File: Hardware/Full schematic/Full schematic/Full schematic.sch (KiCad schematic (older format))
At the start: 145 parts, among them J1 Conn_01x04_Male, J4 Conn_01x02_Male, J6 Conn_01x02_Male, J7 Conn_01x02_Male, J8 Conn_01x07_Male, K1 EDR101A0500, K2 EDR101A0500, K3 EDR101A0500, K4 EDR101A0500, K5 EDR101A0500, K6 EDR101A0500, Q1 BSS138, Q2 IRF610, Q3 IRLML2502, Q4 IRLML2502, Q5 IRLML2502, Q6 IRLML2502, Q7 IRLML2502, Q8 IRLML2502, U1 74LVC2T45DC, U2 74LVC2T45DC, U3 AD9835, X1 50MHz

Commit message: 144MHz preamp is ready
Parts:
- added C?: 1nF, symbol Device:C
- added C?: 75pF, symbol Device:C
- added L?: 200nH, symbol Device:L
- added Q?: BFS17, symbol Device:Q_NPN_BEC
- added R?: 1k, symbol Device:R
- added R?: 6.2k, symbol Device:R
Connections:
- wire segments 369 -> 385
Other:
- note added: "144-146MHz\n1.5V P-P\n8.5mW @ 33 Ohm"
- note added: "200V P-P at antenna equivalent.\nAntenna equivalent is 240 Ohm resistor\nin series with 35pF capacitor."
- note added: "4.32V P-P\n@\n10 Ohm"
- note added: "6T\nD5\nd0.5"
- note added: "M50BH\n20x12x6 ring"
- note removed: "144-146MHz 1.5V P-P"
- note removed: "200V P-P at antenna equivalent.\nAntenna equivalent is 240 Ohm resistor\nin series with 35pF capacitor.\n\nDesired (3W) is 38V P-P at R, 243V P-P at antenna equivalent.\n\nWith this equivalent resonance is achieved at 70pF."
- moved on the sheet: C?, J?, Q?, R?, U?

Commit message: Second prototype PCB is almost ready
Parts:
- removed J4: Conn_01x02_Male, Connector_PinHeader_2.54mm:PinHeader_1x02_P2.54mm_Vertical, symbol Connector:Conn_01x02_Male
- removed J?: Conn_01x02_Male, symbol Connector:Conn_01x02_Male
- added C28, C41, C42: 1nF, Capacitor_SMD:C_0805_2012Metric_Pad1.18x1.45mm_HandSolder, symbol Device:C
- added C43: 0.1uF, Capacitor_SMD:C_0805_2012Metric_Pad1.18x1.45mm_HandSolder, symbol Device:C
- added C44: 20pF, Capacitor_SMD:C_0805_2012Metric_Pad1.18x1.45mm_HandSolder, symbol Device:C
- added C51: 470uF x 10V, Capacitor_THT:CP_Radial_D8.0mm_P3.80mm, symbol Device:CP
- added C54: 56pF, Capacitor_SMD:C_0805_2012Metric_Pad1.18x1.45mm_HandSolder, symbol Device:C
- added J3, J8: Conn_01x02_Male, Connector_PinHeader_2.54mm:PinHeader_1x02_P2.54mm_Vertical, symbol Connector:Conn_01x02_Male
- added J5: Conn_01x03_Male, Connector_PinHeader_2.54mm:PinHeader_1x03_P2.54mm_Vertical, symbol Connector:Conn_01x03_Male
- added L8: 300nH, Inductor_THT:L_Axial_L16.0mm_D7.5mm_P7.62mm_Vertical_Fastron_XHBCC, symbol Device:L
- added L9: 23.5nH, Inductor_THT:L_Axial_L9.5mm_D4.0mm_P5.08mm_Vertical_Fastron_SMCC, symbol Device:L
- added Q7: AFT05MS003N, Package_TO_SOT_SMD:SOT-89-3_Handsoldering, symbol Device:Q_NMOS_GSD
- added RV2: 20k, Potentiometer_THT:Potentiometer_Bourns_3386C_Horizontal, symbol Device:R_POT
- C10, C12: footprint Capacitor_THT:CP_Radial_D10.0mm_P5.00mm -> Capacitor_THT:CP_Radial_D8.0mm_P3.80mm
- C16, C20, C21, C23, C24, C31, C33, C34: renamed from C?; footprint (none) -> Capacitor_SMD:C_0805_2012Metric_Pad1.18x1.45mm_HandSolder
- C19, C32, C52: renamed from C?; footprint (none) -> Capacitor_THT:CP_Radial_D8.0mm_P3.80mm
- C25: renamed from C20; footprint Capacitor_THT:CP_Radial_D14.0mm_P7.50mm -> Capacitor_THT:CP_Radial_D10.0mm_P5.00mm
- J2: renamed from J?; footprint (none) -> Connector_PinHeader_2.54mm:PinHeader_1x03_P2.54mm_Vertical
- J4: renamed from J?; footprint (none) -> Connector_PinHeader_2.54mm:PinHeader_1x04_P2.54mm_Vertical
- J9: renamed from J8; footprint (none) -> Connector_PinHeader_2.54mm:PinHeader_1x07_P2.54mm_Vertical
- L6: footprint Inductor_THT:L_Radial_D9.5mm_P5.00mm_Fastron_07HVP -> Inductor_THT:L_Toroid_Vertical_L21.6mm_W9.1mm_P8.40mm_Bourns_5700
- L7: renamed from L?; footprint (none) -> Inductor_THT:L_Axial_L5.3mm_D2.2mm_P7.62mm_Horizontal_Vishay_IM-1
- Q4: renamed from Q2; footprint Package_TO_SOT_THT:TO-220-3_Horizontal_TabDown -> Package_TO_SOT_THT:TO-220-3_Vertical
- Q6: renamed from Q?; footprint (none) -> Package_TO_SOT_SMD:SOT-23
- R10, R11, R13, R14, R16, R17, R18, R19, R22, R23, R24, R25, R29, R31, R32: renamed from R?; footprint (none) -> Resistor_SMD:R_0805_2012Metric_Pad1.20x1.40mm_HandSolder
- U1, U2: footprint Package_SO:SSOP-8_3.9x5.05mm_P1.27mm -> Package_SO:SSOP-8_2.95x2.8mm_P0.65mm
- U4: renamed from U?; footprint (none) -> Package_SO:SOIC-8_5.23x5.23mm_P1.27mm
- gave numbers to parts that had none: 3
- renumbered C15 to C14, C16 to C15, C19 to C18, C18 to C22, C21 to C26, C22 to C27, C23 to C29, C24 to C30, C25 to C35, C26 to C36, C27 to C37, C28 to C38, C29 to C39, C30 to C40, C31 to C45, C32 to C46, C33 to C47, C34 to C48, C35 to C49, C36 to C50, C37 to C53, C38 to C55, C39 to C56, C40 to C57, C41 to C58, C42 to C59, C43 to C60, C44 to C61, C45 to C62, C46 to C63, C47 to C64, C48 to C65, C49 to C66, C50 to C67, C51 to C68, C52 to C69, C53 to C70, C54 to C71, C55 to C72, C56 to C73, C57 to C74, C58 to C75, C59 to C76, C60 to C77, C61 to C78, Q5 to Q10, Q6 to Q11, Q7 to Q12, Q8 to Q13, Q1 to Q2, Q3 to Q8, Q4 to Q9, R10 to R12, R11 to R15, R12 to R20, R13 to R21, R14 to R26, R15 to R27, R16 to R28, R17 to R30, R18 to R33, R19 to R34, R20 to R35, R21 to R36, R22 to R37, R23 to R38, R5 to R4, R6 to R5, R4 to R6
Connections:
- net labels added: Manipulation, PWR_144_OUT, PWR_CMN_3.3, PWR_CMN_5
- net labels removed: +3.3V, +5V
- wire segments 385 -> 423
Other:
- note added: "3T\nD3\nd1.0"
- note added: "8T\nD7\nd1.0"
- note added: "Power - 144MHz"
- note added: "To 144MHz 50 Ohm antenna"
- note added: "To 3.5MHz antenna"
- note removed: "Manipulation\nand\nModulation\n1 - OFF\n0 - ON"
- note removed: "To antenna"
- moved on the sheet: C1, C10, C11, C12, C13, C14, C15, C16, C17, C18, C19, C2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

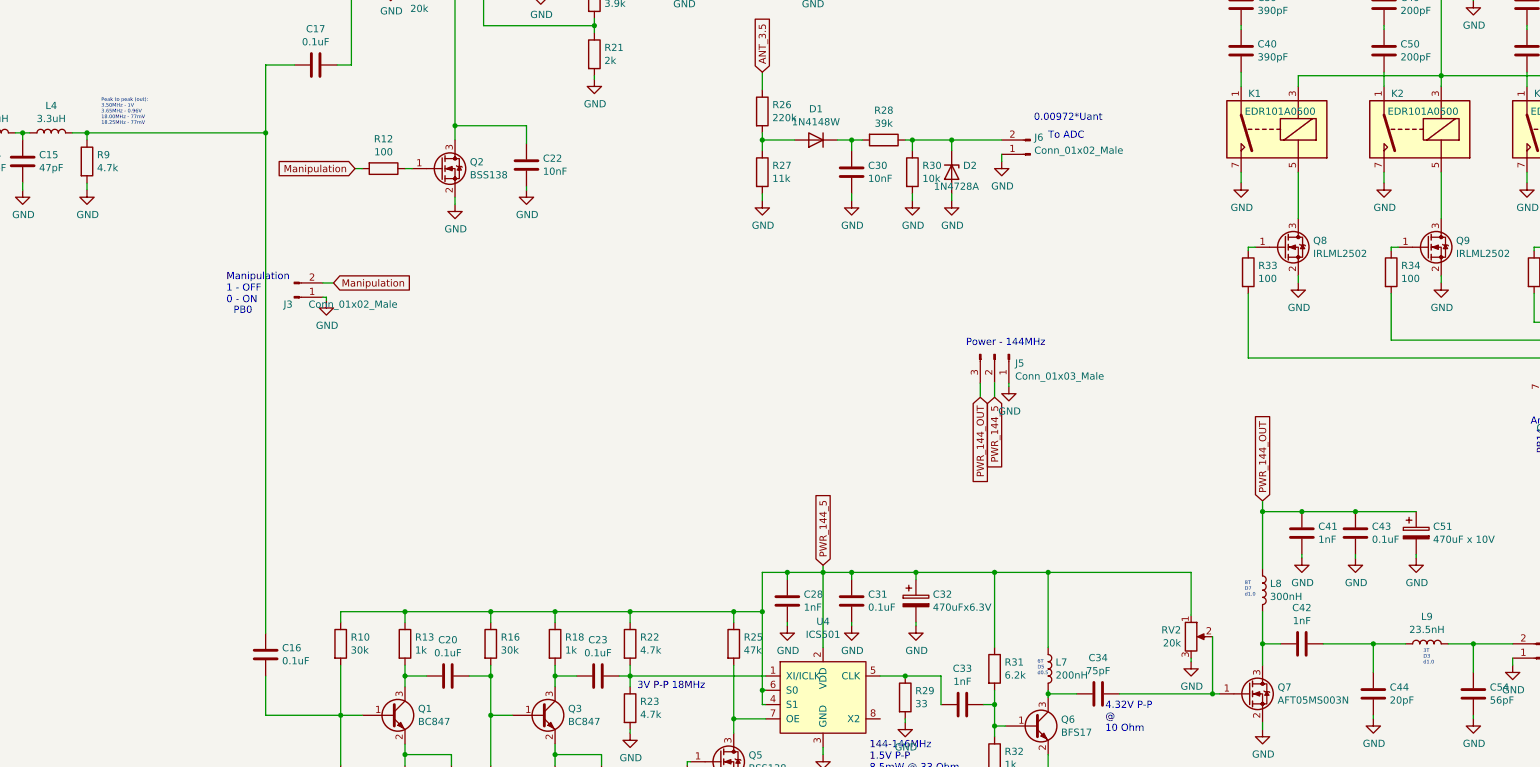
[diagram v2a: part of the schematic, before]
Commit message: 144MHz part is ready except antenna
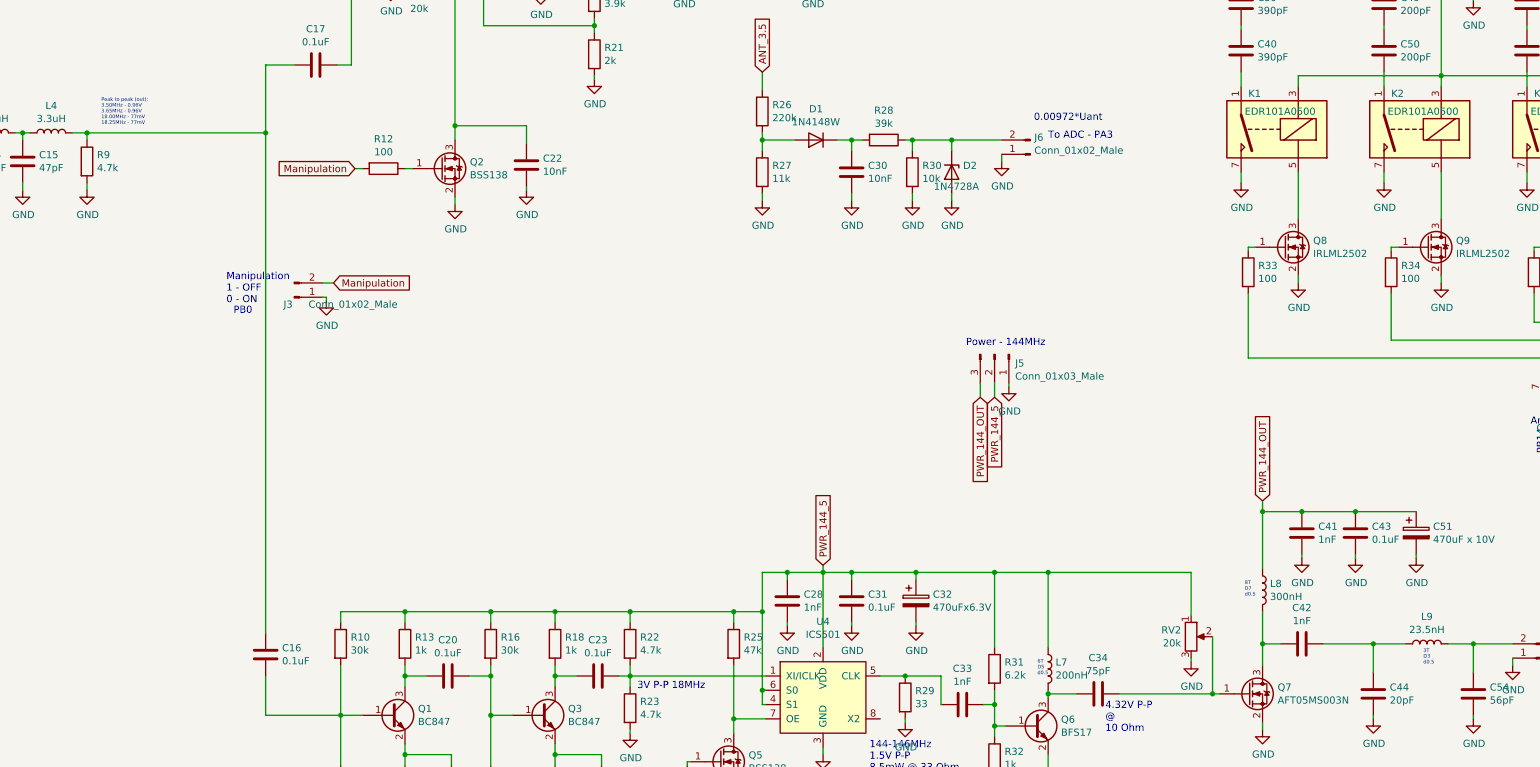
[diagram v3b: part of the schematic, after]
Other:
- note added: "3T\nD3\nd0.5"
- note added: "8T\nD7\nd0.5"
- note added: "Peak to peak (out):\n3.50MHz - 0.96V\n3.65MHz - 0.96V\n18.00MHz - 77mV\n18.25MHz - 77mV"
- note added: "To ADC - PA3"
- note removed: "3T\nD3\nd1.0"
- note removed: "8T\nD7\nd1.0"
- note removed: "Peak to peak (out):\n3.50MHz - 1V\n3.65MHz - 0.96V\n18.00MHz - 77mV\n18.25MHz - 77mV"
- note removed: "To ADC"
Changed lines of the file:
@@
 	7075 3725 7025 3725
 Text Notes 8775 3675 0    25   ~ 0
-Peak to peak (out):\n3.50MHz - 1V\n3.65MHz - 0.96V\n18.00MHz - 77mV\n18.25MHz - 77mV
+Peak to peak (out):\n3.50MHz - 0.96V\n3.65MHz - 0.96V\n18.00MHz - 77mV\n18.25MHz - 77mV
 $Comp
 L power:GND #PWR025
@@
 	15075 3925 15075 3875
 Text Notes 15400 3775 0    50   ~ 0
-To ADC
+To ADC - PA3
 $Comp
 L Diode:1N47xxA D2
@@
 To 144MHz 50 Ohm antenna
 Text Notes 16775 6975 0    25   ~ 0
-8T\nD7\nd1.0
+8T\nD7\nd0.5
 Text Notes 18025 7450 0    25   ~ 0
-3T\nD3\nd1.0
+3T\nD3\nd0.5
 $Comp
 L Device:C C28

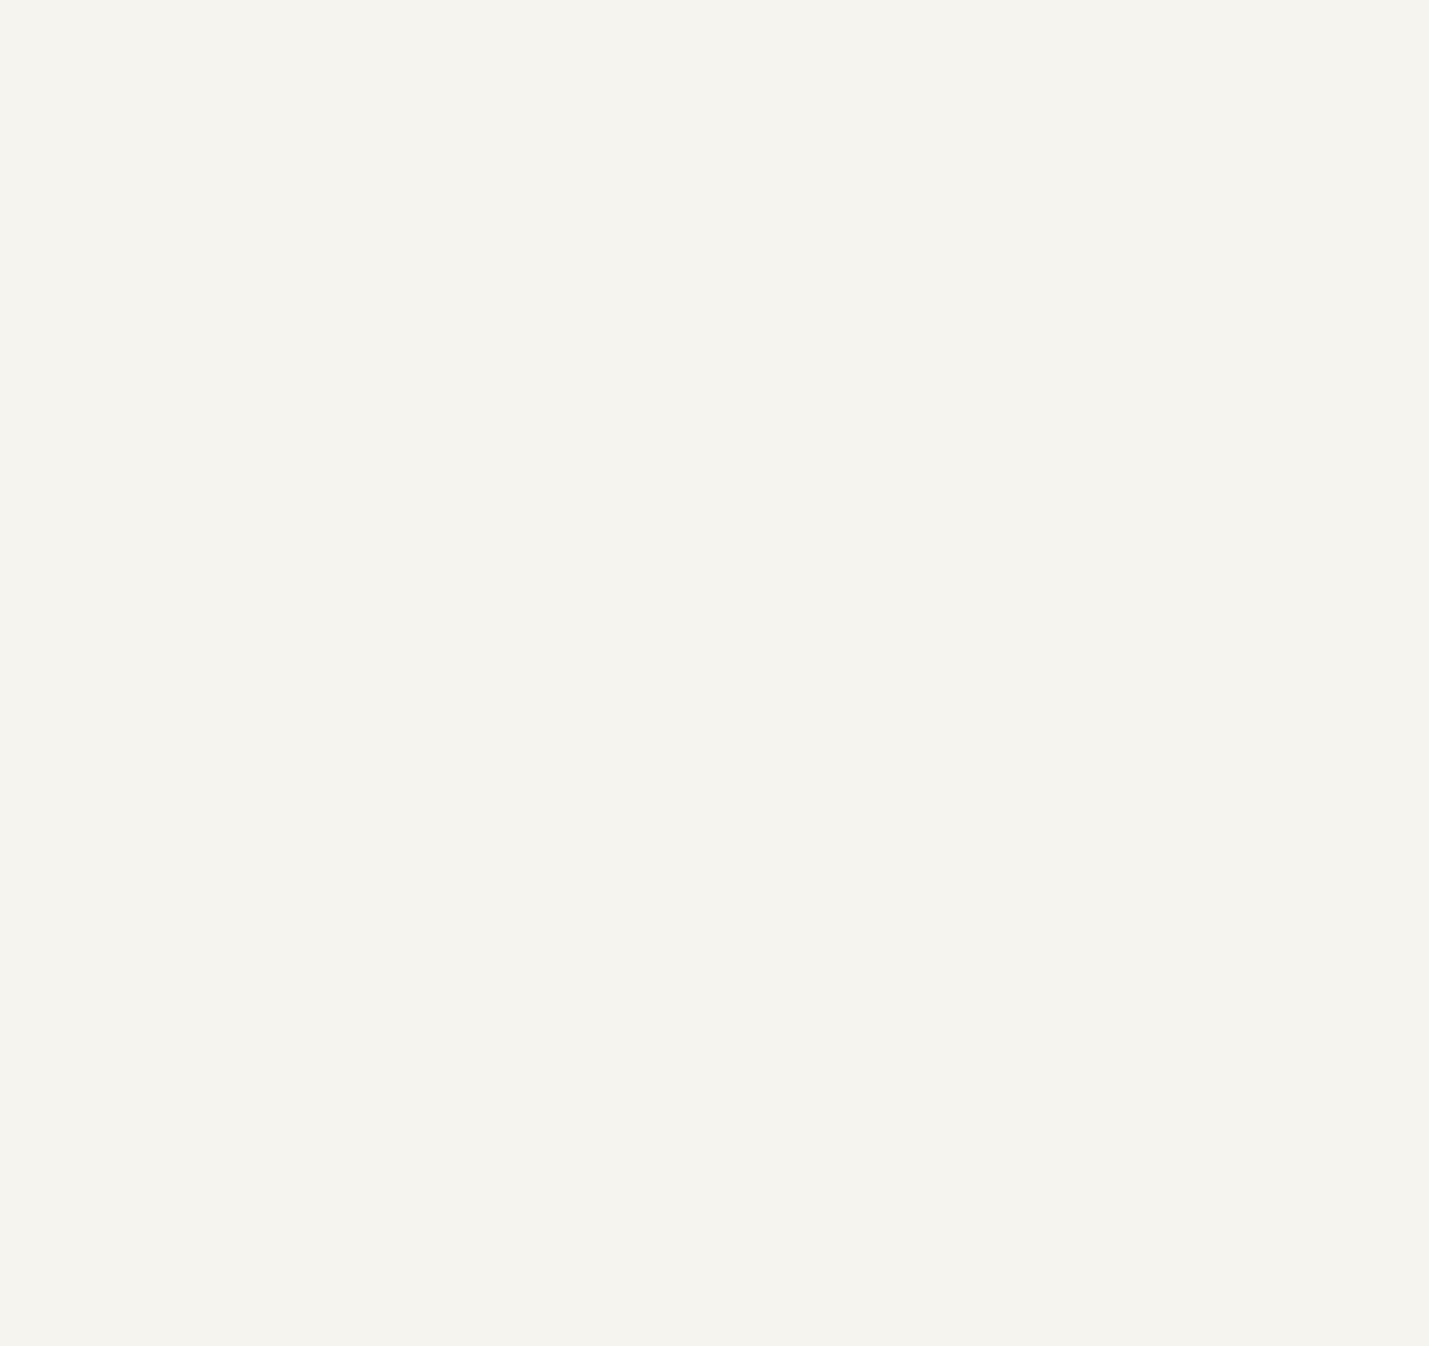
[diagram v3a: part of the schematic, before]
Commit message: Second I2C added, ready for 24c256 driver
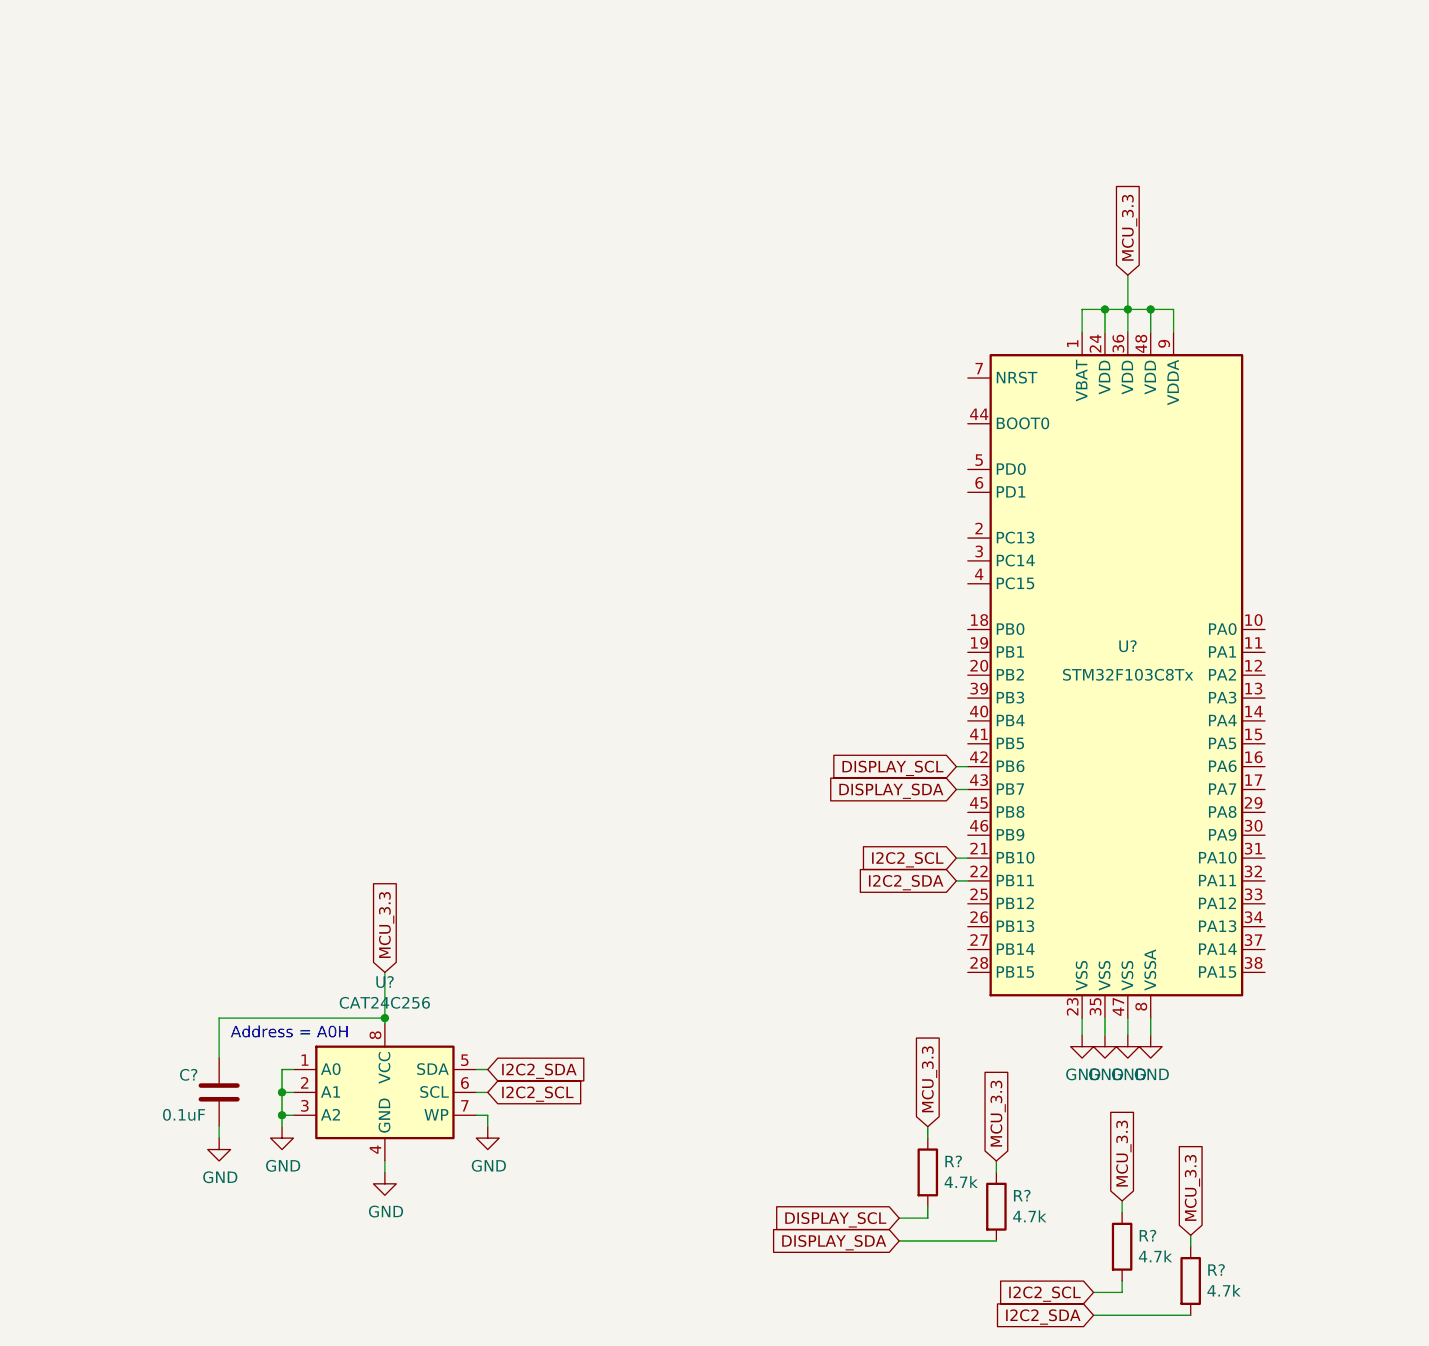
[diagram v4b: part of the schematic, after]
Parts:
- added C?: 0.1uF, symbol Device:C
- added R? (x4): 4.7k, symbol Device:R
- added U?: STM32F103C8Tx, Package_QFP:LQFP-48_7x7mm_P0.5mm, symbol MCU_ST_STM32F1:STM32F103C8Tx
- added U?: CAT24C256, symbol Memory_EEPROM:CAT24C256
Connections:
- net GND: now also C?.1, U?.1 (A0), U?.2 (A1), U?.23 (VSS), U?.3 (A2), U?.35 (VSS), U?.4 (GND), U?.47 (VSS), U?.7 (WP), U?.8 (VSSA)
- new net DISPLAY_SCL: R?.2, U?.42 (PB6)
- new net DISPLAY_SDA: R?.2, U?.43 (PB7)
- new net I2C2_SCL: R?.2, U?.21 (PB10), U?.6 (SCL)
- new net I2C2_SDA: R?.2, U?.22 (PB11), U?.5 (SDA)
- new net MCU_3.3: C?.2, R?.1, R?.1, R?.1, R?.1, U?.1 (VBAT), U?.24 (VDD), U?.36 (VDD), U?.48 (VDD), U?.8 (VCC), U?.9 (VDDA)
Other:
- note added: "Address = A0H"
